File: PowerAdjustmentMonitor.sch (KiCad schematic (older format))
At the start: 18 parts, among them U3 LM317T, U4 7805, U5 7805, U6 LM317T, U7 LM324

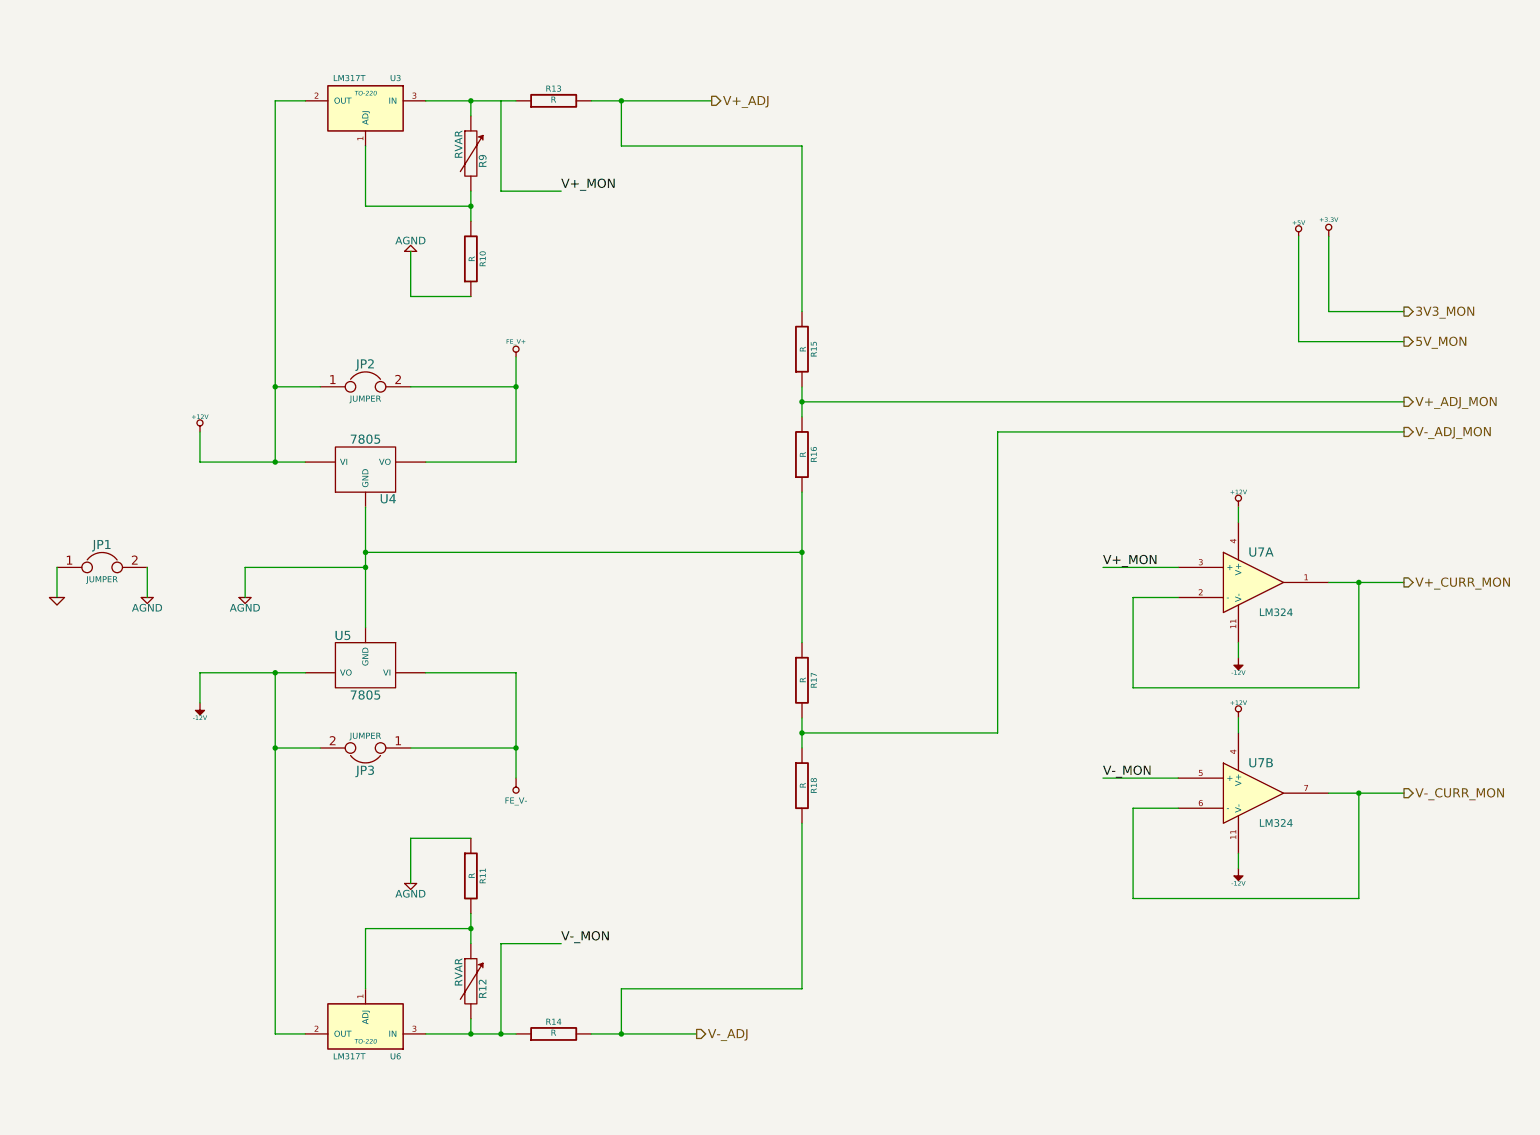
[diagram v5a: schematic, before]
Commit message: Associated and placed the Power Modification Module
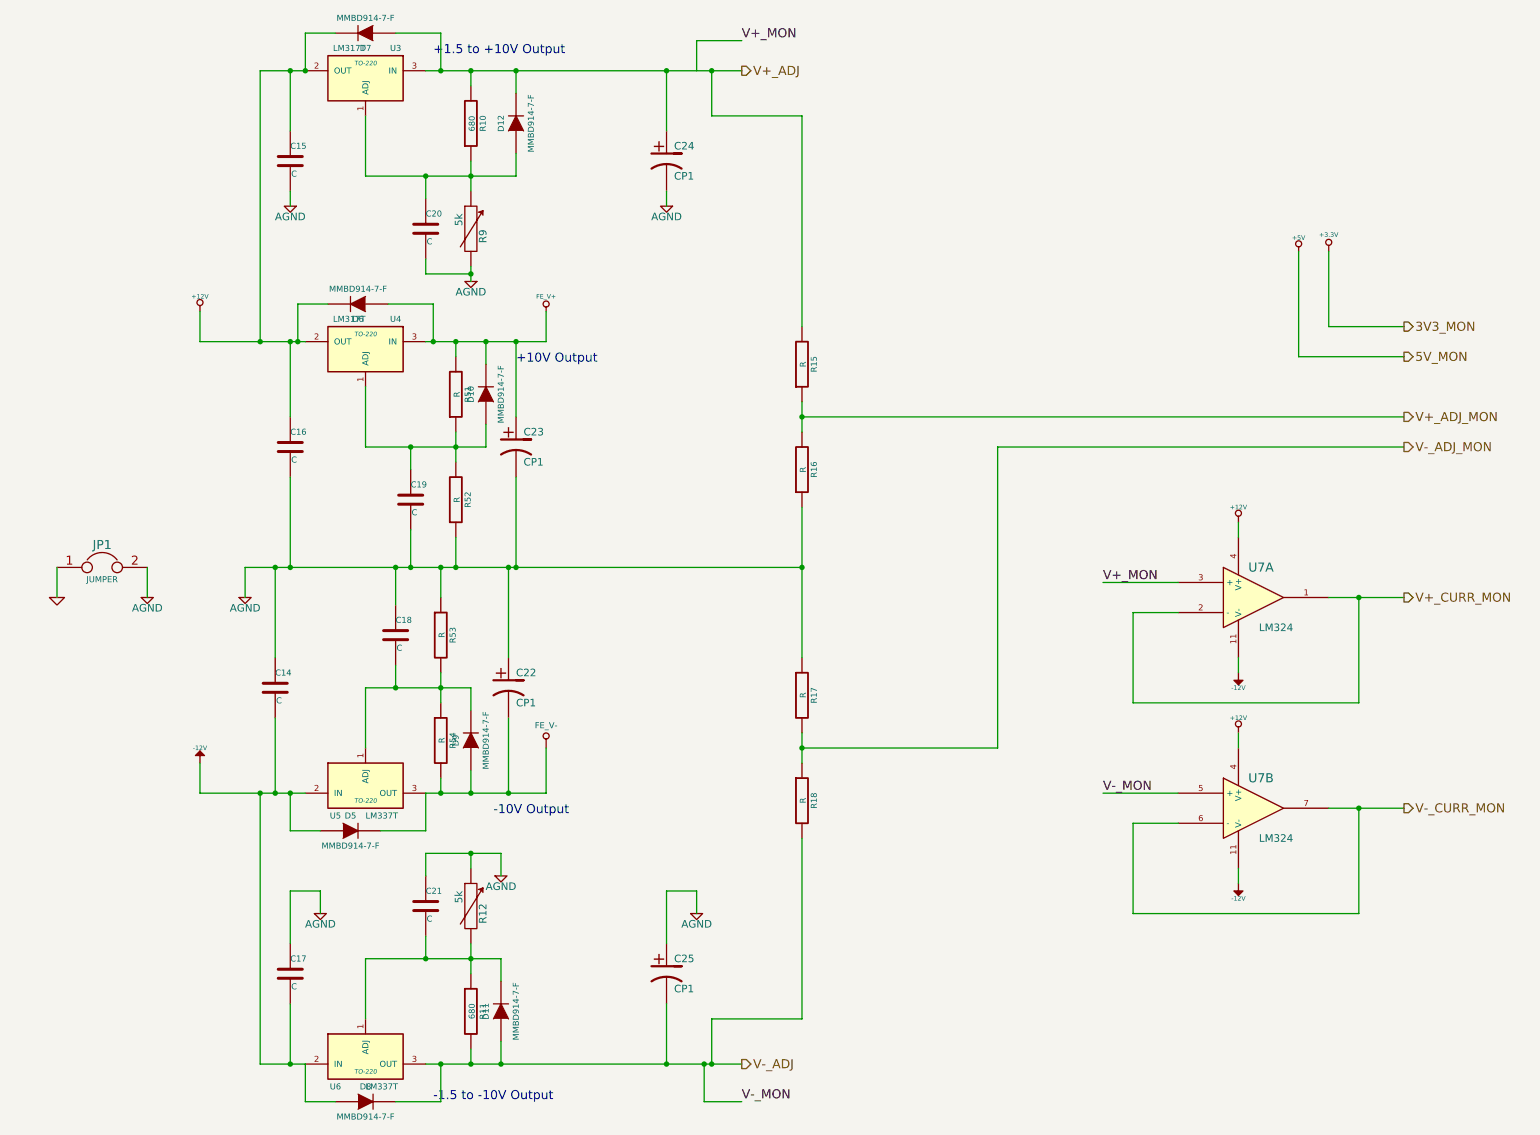
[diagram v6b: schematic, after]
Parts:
- removed JP2, JP3: JUMPER, symbol JUMPER
- removed R13, R14: R, symbol R
- removed U4, U5: 7805, symbol 7805
- removed U6: LM317T, TO-220, symbol LM317T
- added C14, C15, C16, C17, C18, C19, C20, C21: C, symbol C
- added C22, C23, C24, C25: CP1, symbol CP1
- added D10, D11, D12, D5, D6, D7, D8, D9: MMBD914-7-F, symbol DIODE
- added R51, R52, R53, R54: R, symbol R
- added U4: LM317T, TO-220, symbol LM317T
- added U5, U6: LM337T, TO-220, symbol LM337T
- R10, R11: value R -> 680
- R12, R9: value RVAR -> 5k
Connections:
- net +12V: now also C15.1, C16.1, D6.2 (K), D7.2 (K), U4.2 (OUT)
- net -12V: now also C14.2, C17.2, D5.1 (A), D8.1 (A), U5.2 (IN), U6.2 (IN)
- net AGND: now also R12.1, R9.2, C14.1, C15.2, C16.2, C17.1, C18.1, C19.2, C20.2, C21.1, C22.1, C23.2, C24.2, C25.1, R52.1, R53.1; no longer R10.1, R11.1
- net FE_V+: now also C23.1, D10.2 (K), D6.1 (A), R51.2, U4.3 (IN)
- net FE_V-: now also C22.2, D5.2 (K), D9.1 (A), R54.2, U5.3 (OUT)
- net V+_ADJ: now also R10.2, U3.3 (IN), C24.1, D12.2 (K), D7.1 (A)
- net V-_ADJ: now also R11.2, U7.5 (+), C25.2, D11.1 (A), D8.2 (K), U6.3 (OUT)
- net at R9.1: now also R10.1, U3.1 (ADJ), C20.1, D12.1 (A); no longer U3.3 (IN)
- net V-_MON: no longer names the net of R12.2
- net V-_MON: now also R11.1, C21.2, D11.2 (K), U6.1 (ADJ); no longer U7.5 (+)
- new net: C19.1, D10.1 (A), R51.1, R52.2, U4.1 (ADJ)
- new net: C18.2, D9.2 (K), R53.2, R54.1, U5.1 (ADJ)
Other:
- note added: "+1.5 to +10V Output"
- note added: "+10V Output"
- note added: "-1.5 to -10V Output"
- note added: "-10V Output"
- moved on the sheet: R10, R11, R12, R15, R16, R17, R18, R9, U3, U7A, U7B

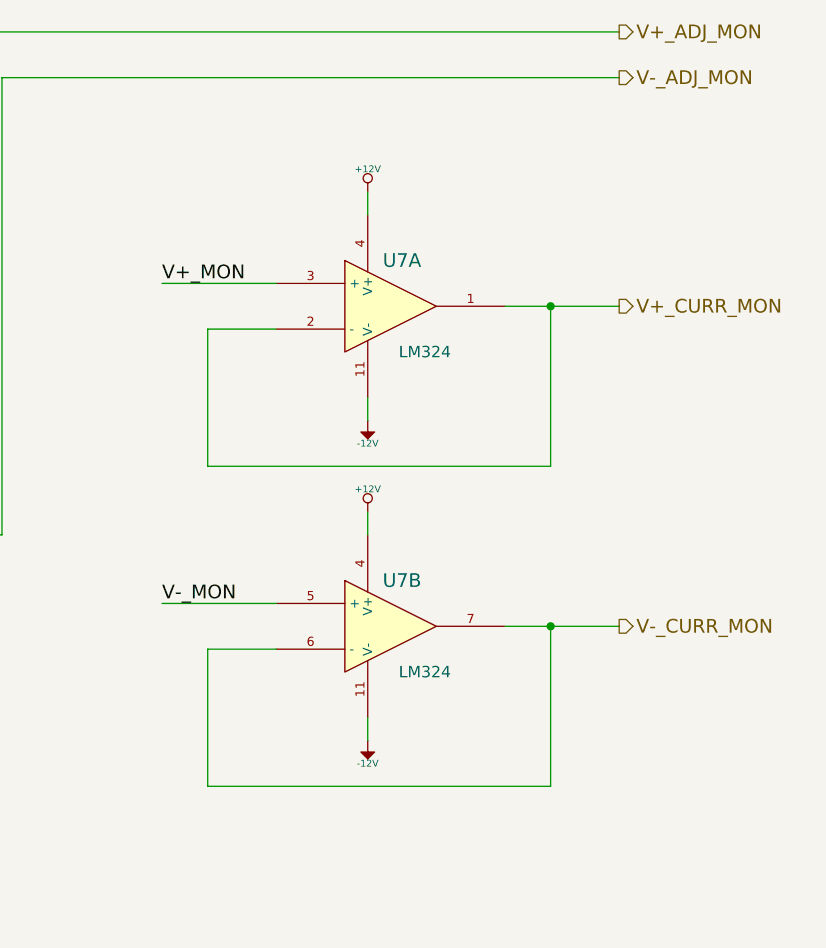
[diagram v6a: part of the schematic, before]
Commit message: Associated and placed the LED Driver Module
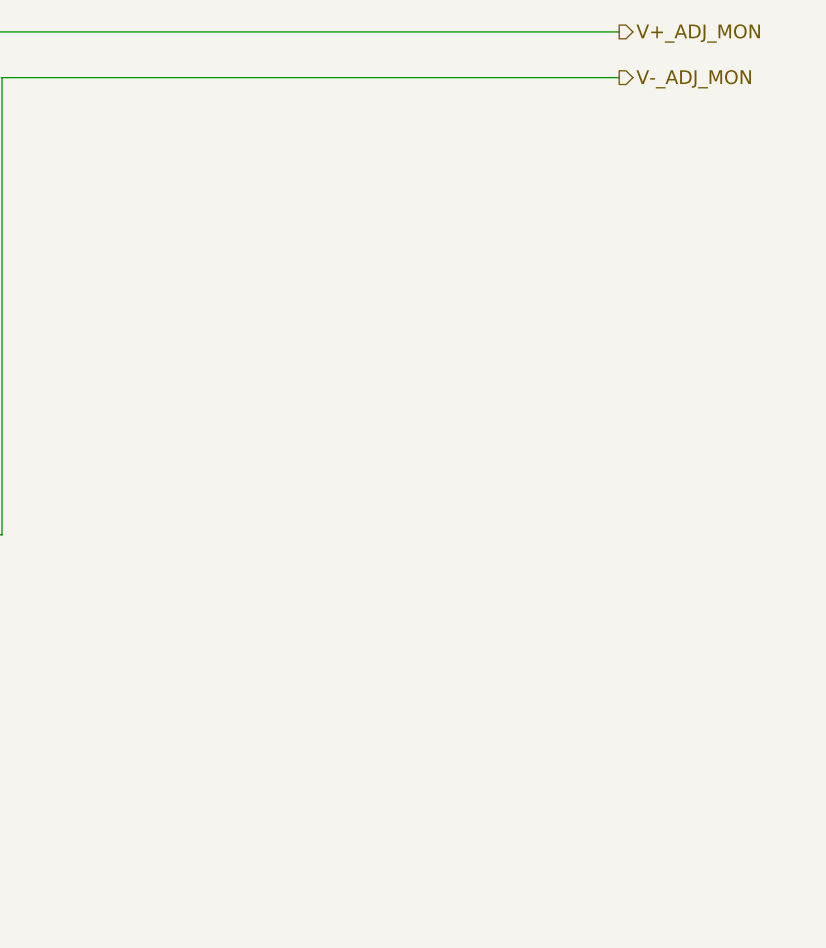
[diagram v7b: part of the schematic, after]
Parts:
- removed U7: LM324, symbol LM324
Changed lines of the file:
@@
 $EndDescr
 $Comp
-L +3.3V #PWR44
+L +3.3V #PWR025
 U 1 1 52F2A379
 P 9700 2000
-F 0 "#PWR44" H 9700 1960 30  0001 C CNN
+F 0 "#PWR025" H 9700 1960 30  0001 C CNN
 F 1 "+3.3V" H 9700 2110 30  0000 C CNN
 F 2 "" H 9700 2000 60  0000 C CNN
@@
 $EndComp
 $Comp
-L +5V #PWR43
+L +5V #PWR026
 U 1 1 52F2A37F
 P 9500 2000
-F 0 "#PWR43" H 9500 2090 20  0001 C CNN
+F 0 "#PWR026" H 9500 2090 20  0001 C CNN
 F 1 "+5V" H 9500 2090 30  0000 C CNN
 F 2 "" H 9500 2000 60  0000 C CNN
@@
 $EndComp
 $Comp
-L +12V #PWR28
+L +12V #PWR027
 U 1 1 52F2A40B
 P 2200 2400
-F 0 "#PWR28" H 2200 2350 20  0001 C CNN
+F 0 "#PWR027" H 2200 2350 20  0001 C CNN
 F 1 "+12V" H 2200 2500 30  0000 C CNN
 F 2 "" H 2200 2400 60  0000 C CNN
@@
 $EndComp
 $Comp
-L -12V #PWR29
+L -12V #PWR028
 U 1 1 52F2A411
 P 2200 5400
-F 0 "#PWR29" H 2200 5530 20  0001 C CNN
+F 0 "#PWR028" H 2200 5530 20  0001 C CNN
 F 1 "-12V" H 2200 5500 30  0000 C CNN
 F 2 "" H 2200 5400 60  0000 C CNN
@@
 $EndComp
 $Comp
-L GND #PWR26
+L GND #PWR029
 U 1 1 52F2A4F6
 P 1250 4300
-F 0 "#PWR26" H 1250 4300 30  0001 C CNN
+F 0 "#PWR029" H 1250 4300 30  0001 C CNN
 F 1 "GND" H 1250 4230 30  0001 C CNN
 F 2 "" H 1250 4300 60  0000 C CNN
@@
 $EndComp
 $Comp
-L AGND #PWR27
+L AGND #PWR030
 U 1 1 52F2A718
 P 1850 4300
-F 0 "#PWR27" H 1850 4300 40  0001 C CNN
+F 0 "#PWR030" H 1850 4300 40  0001 C CNN
 F 1 "AGND" H 1850 4230 50  0000 C CNN
 F 2 "" H 1850 4300 60  0000 C CNN
@@
 $EndComp
 $Comp
-L AGND #PWR30
+L AGND #PWR031
 U 1 1 52F2A798
 P 2500 4300
-F 0 "#PWR30" H 2500 4300 40  0001 C CNN
+F 0 "#PWR031" H 2500 4300 40  0001 C CNN
 F 1 "AGND" H 2500 4230 50  0000 C CNN
 F 2 "" H 2500 4300 60  0000 C CNN
@@
 $EndComp
 $Comp
-L FE_V+ #PWR35
+L FE_V+ #PWR032
 U 1 1 52F2A802
 P 4500 2400
-F 0 "#PWR35" H 4500 2500 30  0001 C CNN
+F 0 "#PWR032" H 4500 2500 30  0001 C CNN
 F 1 "FE_V+" H 4500 2500 30  0000 C CNN
 F 2 "" H 4500 2400 60  0000 C CNN
@@
 $EndComp
 $Comp
-L AGND #PWR38
+L AGND #PWR033
 U 1 1 52F2A9E8
 P 5500 6400
-F 0 "#PWR38" H 5500 6400 40  0001 C CNN
+F 0 "#PWR033" H 5500 6400 40  0001 C CNN
 F 1 "AGND" H 5500 6330 50  0000 C CNN
 F 2 "" H 5500 6400 60  0000 C CNN
@@
 $EndComp
 $Comp
-L AGND #PWR33
+L AGND #PWR034
 U 1 1 52F2AAAD
 P 4000 2200
-F 0 "#PWR33" H 4000 2200 40  0001 C CNN
+F 0 "#PWR034" H 4000 2200 40  0001 C CNN
 F 1 "AGND" H 4000 2130 50  0000 C CNN
 F 2 "" H 4000 2200 60  0000 C CNN
@@
 Text HLabel 10200 3300 2    60   Output ~ 0
 V-_ADJ_MON
-Text HLabel 10200 4300 2    60   Output ~ 0
-V+_CURR_MON
-Text HLabel 10200 5700 2    60   Output ~ 0
-V-_CURR_MON
 $Comp
 L R R15
@@
 V+_MON
 $Comp
-L LM324 U7
-U 1 1 52F2B56C
-P 9200 4300
-F 0 "U7" H 9250 4500 60  0000 C CNN
-F 1 "LM324" H 9350 4100 50  0000 C CNN
-F 2 "" H 9200 4300 60  0000 C CNN
-F 3 "" H 9200 4300 60  0000 C CNN
-	1    9200 4300
-	1    0    0    -1
-$EndComp
-$Comp
-L -12V #PWR40
-U 1 1 52F2B572
-P 9100 4800
-F 0 "#PWR40" H 9100 4930 20  0001 C CNN
-F 1 "-12V" H 9100 4900 30  0000 C CNN
-F 2 "" H 9100 4800 60  0000 C CNN
-F 3 "" H 9100 4800 60  0000 C CNN
-	1    9100 4800
-	1    0    0    1
-$EndComp
-$Comp
-L +12V #PWR39
-U 1 1 52F2B578
-P 9100 3800
-F 0 "#PWR39" H 9100 3750 20  0001 C CNN
-F 1 "+12V" H 9100 3900 30  0000 C CNN
-F 2 "" H 9100 3800 60  0000 C CNN
-F 3 "" H 9100 3800 60  0000 C CNN
-	1    9100 3800
-	-1   0    0    -1
-$EndComp
-$Comp
-L LM324 U7
-U 2 1 52F2B580
-P 9200 5700
-F 0 "U7" H 9250 5900 60  0000 C CNN
-F 1 "LM324" H 9350 5500 50  0000 C CNN
-F 2 "" H 9200 5700 60  0000 C CNN
-F 3 "" H 9200 5700 60  0000 C CNN
-	2    9200 5700
-	1    0    0    -1
-$EndComp
-$Comp
-L -12V #PWR42
-U 1 1 52F2B586
-P 9100 6200
-F 0 "#PWR42" H 9100 6330 20  0001 C CNN
-F 1 "-12V" H 9100 6300 30  0000 C CNN
-F 2 "" H 9100 6200 60  0000 C CNN
-F 3 "" H 9100 6200 60  0000 C CNN
-	1    9100 6200
-	1    0    0    1
-$EndComp
-$Comp
-L +12V #PWR41
-U 1 1 52F2B58C
-P 9100 5200
-F 0 "#PWR41" H 9100 5150 20  0001 C CNN
-F 1 "+12V" H 9100 5300 30  0000 C CNN
-F 2 "" H 9100 5200 60  0000 C CNN
-F 3 "" H 9100 5200 60  0000 C CNN
-	1    9100 5200
-	-1   0    0    -1
-$EndComp
-Text Label 8200 4200 0    60   ~ 0
-V+_MON
-Text Label 8200 5600 0    60   ~ 0
-V-_MON
-$Comp
 L RVAR R12
 U 1 1 52F2B933
@@
 	5500 600  5800 600
 Wire Wire Line
-	9100 3800 9100 3900
-Wire Wire Line
-	9100 4700 9100 4800
-Wire Wire Line
-	9100 5200 9100 5300
-Wire Wire Line
-	9100 6100 9100 6200
-Wire Wire Line
-	9700 4300 10200 4300
-Wire Wire Line
-	9700 5700 10200 5700
-Wire Wire Line
-	9900 4300 9900 5000
-Wire Wire Line
-	9900 5000 8400 5000
-Wire Wire Line
-	8400 5000 8400 4400
-Wire Wire Line
-	8400 4400 8700 4400
-Connection ~ 9900 4300
-Wire Wire Line
-	9900 5700 9900 6400
-Wire Wire Line
-	9900 6400 8400 6400
-Wire Wire Line
-	8400 6400 8400 5800
-Wire Wire Line
-	8400 5800 8700 5800
-Connection ~ 9900 5700
-Wire Wire Line
-	8700 5600 8200 5600
-Wire Wire Line
-	8700 4200 8200 4200
-Wire Wire Line
 	10200 3100 6200 3100
 Connection ~ 6200 4100
@@
 	4000 2100 4000 2200
 $Comp
-L AGND #PWR31
+L AGND #PWR035
 U 1 1 530A4A4A
 P 2800 1700
-F 0 "#PWR31" H 2800 1700 40  0001 C CNN
+F 0 "#PWR035" H 2800 1700 40  0001 C CNN
 F 1 "AGND" H 2800 1630 50  0000 C CNN
 F 2 "" H 2800 1700 60  0000 C CNN
@@
 	2800 1700 2800 1600
 $Comp
-L AGND #PWR37
+L AGND #PWR036
 U 1 1 530A4AF9
 P 5300 1700
-F 0 "#PWR37" H 5300 1700 40  0001 C CNN
+F 0 "#PWR036" H 5300 1700 40  0001 C CNN
 F 1 "AGND" H 5300 1630 50  0000 C CNN
 F 2 "" H 5300 1700 60  0000 C CNN
@@
 	5300 6250 5300 6600
 $Comp
-L AGND #PWR32
+L AGND #PWR037
 U 1 1 530A4E0D
 P 3000 6400
-F 0 "#PWR32" H 3000 6400 40  0001 C CNN
+F 0 "#PWR037" H 3000 6400 40  0001 C CNN
 F 1 "AGND" H 3000 6330 50  0000 C CNN
 F 2 "" H 3000 6400 60  0000 C CNN
@@
 	2800 6250 2800 6600
 $Comp
-L AGND #PWR34
+L AGND #PWR038
 U 1 1 530A4E16
 P 4200 6150
-F 0 "#PWR34" H 4200 6150 40  0001 C CNN
+F 0 "#PWR038" H 4200 6150 40  0001 C CNN
 F 1 "AGND" H 4200 6080 50  0000 C CNN
 F 2 "" H 4200 6150 60  0000 C CNN
